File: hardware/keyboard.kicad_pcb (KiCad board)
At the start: 2 copper layers, 166 parts, among them J1 USB_OTG, J10 PD5, J11 PD6, J12 PD7, J13 PE6, J14 PF0, J15 PF1, J16 PF4, J17 PF5, J18 PF6, J19 PF7, J2 PB5, J3 PB6, J4 PB7, J5 PC6, J6 PC7, J7 PD2, J8 PD3, J9 PD4, U1 ATMEGA32U4-AU, U2 MCP23018_SSOP, Y1 16MHz

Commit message: Fix diodes, Add board edge
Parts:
- moved J1 77.1 mm to (179.0, 34.1), turned to 180 degrees
- moved F1 69.3 mm to (187.6, 47.8)
- moved C2 67.2 mm to (190.6, 52.6)
- moved S100 59.0 mm to (161.5, 47.4)
- moved U1 54.7 mm to (179.0, 59.6), turned to 180 degrees
- moved J2 51.9 mm to (197.8, 88.8)
- moved C1 32.5 mm to (177.6, 119.4)
- moved U2 31.1 mm to (178.6, 112.8), turned to 90 degrees
- moved R1 27.7 mm to (175.6, 99.4)
- moved D61 13.0 mm to (145.6, 141.5), turned to 350 degrees
- moved D64 12.9 mm to (199.6, 143.7), turned to 10 degrees
- moved D56 2.09 mm to (310.2, 37.9)
- moved D33 2.09 mm to (222.7, 90.0)
- moved D34 2.09 mm to (226.0, 108.8)
- moved D35 2.09 mm to (229.3, 127.5)
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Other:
- board outline added: 321.6 x 127.7 mm

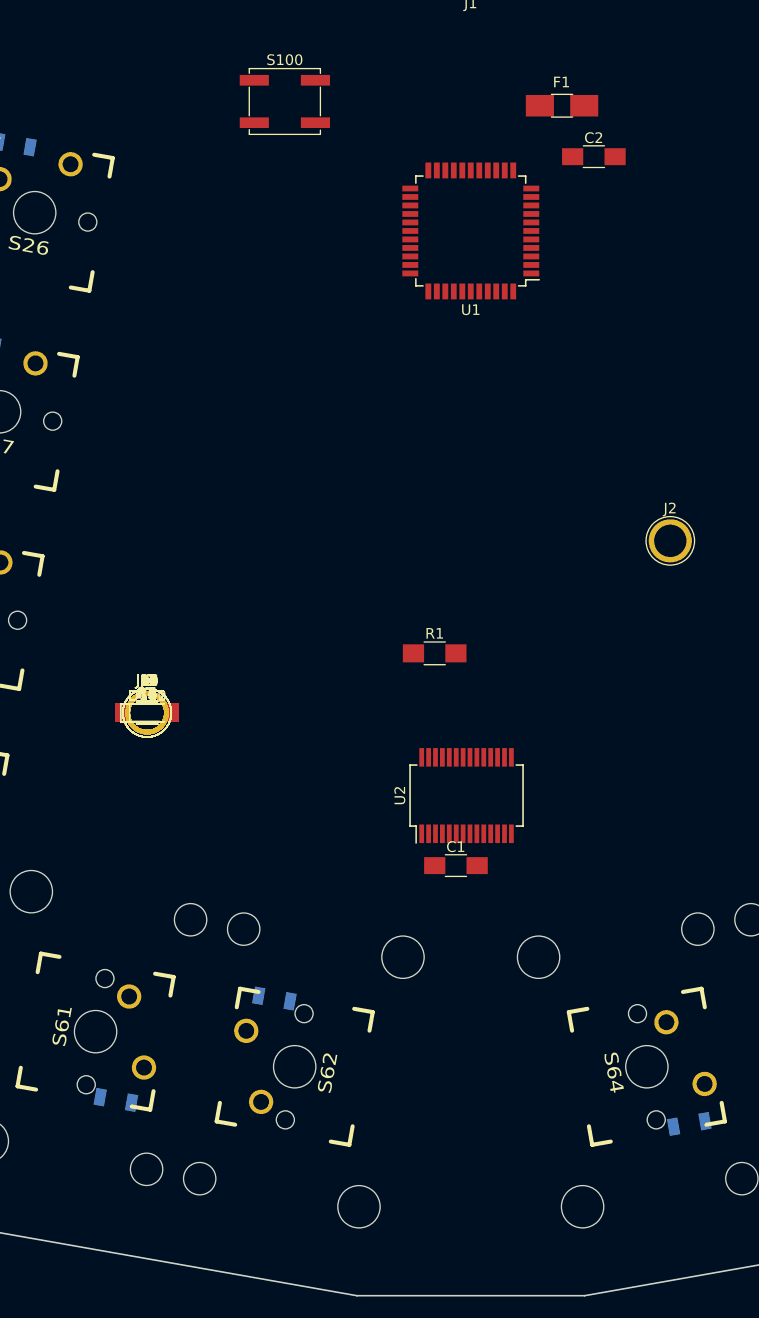
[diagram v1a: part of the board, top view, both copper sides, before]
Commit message: Update expansion pads to be SMD
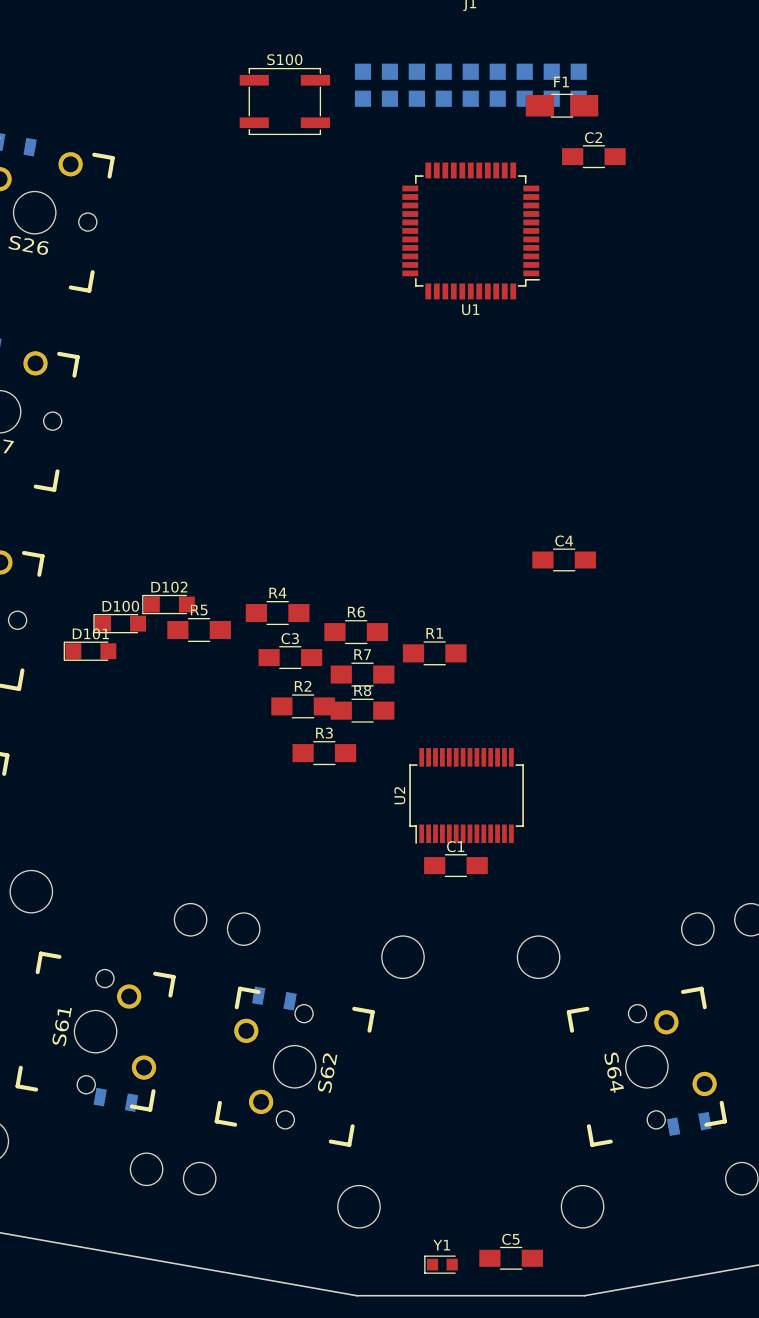
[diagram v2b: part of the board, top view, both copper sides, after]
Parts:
- removed J10: PD5, Connectors:1pin
- removed J11: PD6, Connectors:1pin
- removed J12: PD7, Connectors:1pin
- removed J13: PE6, Connectors:1pin
- removed J14: PF0, Connectors:1pin
- removed J15: PF1, Connectors:1pin
- removed J16: PF4, Connectors:1pin
- removed J17: PF5, Connectors:1pin
- removed J18: PF6, Connectors:1pin
- removed J19: PF7, Connectors:1pin
- removed J3: PB6, Connectors:1pin
- removed J4: PB7, Connectors:1pin
- removed J5: PC6, Connectors:1pin
- removed J6: PC7, Connectors:1pin
- removed J7: PD2, Connectors:1pin
- removed J8: PD3, Connectors:1pin
- removed J9: PD4, Connectors:1pin
- added C4: 100nF, Capacitors_SMD:C_1206_HandSoldering, F.Cu at (187.8, 90.6)
- added C5: 100nF, Capacitors_SMD:C_1206_HandSoldering, F.Cu at (182.8, 156.4)
- J2: value PB5 -> CONN_02X09; footprint Connectors:1pin -> keyboard-modules:pads; moved to B.Cu
- moved Y1 59.0 mm to (176.3, 157.0)
- moved J2 46.9 mm to (179.0, 45.9)
- moved R6 21.1 mm to (168.2, 97.4)
- moved R7 20.6 mm to (168.8, 101.4)
- moved R8 20.3 mm to (168.8, 104.8)
- moved R3 17.1 mm to (165.2, 108.8)
- moved R4 15.5 mm to (160.8, 95.6)
- moved R2 14.7 mm to (163.2, 104.4)
- moved C3 14.5 mm to (162.0, 99.8)
- moved D102 10.4 mm to (150.6, 94.8)
- moved R5 9.21 mm to (153.4, 97.2)
- moved D100 8.77 mm to (146.0, 96.6)
- moved D101 7.86 mm to (143.2, 99.2)
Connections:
- J2 pad 1: /PB5 -> /PF7

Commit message: Add 3d models
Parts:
- J2: moved to F.Cu
- moved C5 159.1 mm to (146.3, 1.59)
- moved Y1 144.4 mm to (206.5, 15.8)
- moved U2 114.8 mm to (136.3, 6.09), turned to 0 degrees
- moved R7 113.2 mm to (203.2, -6.42)
- moved R2 112.7 mm to (204.1, -0.62)
- moved D101 107.4 mm to (203.5, 10.3)
- moved C1 106.2 mm to (194.7, 14.6)
- moved D102 104.3 mm to (203.5, 4.92)
- moved R5 103.8 mm to (197.2, 3.08)
- moved C3 100.8 mm to (190.2, 2.98)
- moved R8 99.7 mm to (183.3, 6.12)
- moved D100 97.9 mm to (201.0, 15.6)
- moved R4 97.9 mm to (183.3, 0.33)
- moved R3 96.8 mm to (187.7, 14.7)
- moved R1 93.1 mm to (197.2, 8.88)
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
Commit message: Start to lay out components
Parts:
- removed D100, D102: LED, LEDs:LED_1206
- D101: value LED -> LED_RGB; footprint LEDs:LED_1206 -> LEDs:LED_RGB_5050-6
- J2: value CONN_02X09 -> CONN_02X10; footprint keyboard-modules:pads -> keyboard-modules:ExpansionPads; moved to B.Cu
- R8: moved to B.Cu
- moved R5 113.0 mm to (171.0, 113.0)
- moved U2 111.6 mm to (179.1, 109.2)
- moved R4 111.0 mm to (171.0, 110.6)
- moved C5 106.4 mm to (171.2, 105.0), turned to 180 degrees
- moved C3 80.2 mm to (169.4, 80.4), turned to 180 degrees
- moved C1 78.9 mm to (180.1, 92.1), turned to 270 degrees
- moved C2 78.8 mm to (177.9, 92.1), turned to 270 degrees
- moved Y1 77.1 mm to (179.0, 87.9), turned to 180 degrees
- moved R8 74.3 mm to (181.9, 80.4), turned to 90 degrees
- moved U1 73.3 mm to (179.5, 80.4)
- moved J2 64.8 mm to (217.2, 37.3), turned to 180 degrees
- moved C4 64.0 mm to (169.4, 77.2), turned to 180 degrees
- moved R7 53.4 mm to (178.8, 41.1), turned to 90 degrees
- moved F1 47.3 mm to (181.9, 41.1), turned to 90 degrees
- moved J1 41.7 mm to (179.1, 34.2), turned to 180 degrees
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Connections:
- net +3V3 renamed Net-(C3-Pad1)
- D101 pad 1: GND -> Net-(D101-Pad1)
- J2 pad 1: /PF7 -> VCC
- J2 pad 10: /PC7 -> /PD2
- J2 pad 11: /PF0 -> /PF1
- J2 pad 12: /PD2 -> /PD3
- J2 pad 13: /PE6 -> /PF0
- J2 pad 14: /PD3 -> /PD4
- J2 pad 15: /PD7 -> /PE6
- J2 pad 16: /PD4 -> /PD5
- J2 pad 17: /PD6 -> /PD7
- J2 pad 18: /PD5 -> /PD6
- J2 pad 2: /PB5 -> GND
- J2 pad 3: /PF6 -> /PF7
- J2 pad 4: /PB6 -> GND
- J2 pad 5: /PF5 -> /PF6
- J2 pad 6: /PB7 -> /PC6
- J2 pad 7: /PF4 -> /PF5
- J2 pad 8: /PC6 -> /PC7
- J2 pad 9: /PF1 -> /PF4
- R1 pad 1: +5V -> Net-(D101-Pad1)
- R1 pad 2: Net-(D100-Pad2) -> GND
- R2 pad 1: (no net) -> Net-(D101-Pad2)
- R2 pad 2: Net-(D101-Pad2) -> GND
- R3 pad 1: (no net) -> Net-(D101-Pad3)
- R3 pad 2: Net-(D102-Pad2) -> GND
- U1 pad 12: /PB7 -> LED3
- U1 pad 29: /PB5 -> LED1
- U1 pad 30: /PB6 -> LED2

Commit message: Start routing
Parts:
- moved S100 3.38 mm to (168.7, 38.6)
- moved R8 0.52 mm to (182.4, 80.5)
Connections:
- U2 pad 17: COL8 -> COL6
- U2 pad 18: COL9 -> COL7
- U2 pad 19: COL10 -> COL8
- U2 pad 20: COL11 -> COL9
- U2 pad 21: COL12 -> COL10
- U2 pad 22: (no net) -> COL11
- U2 pad 23: (no net) -> COL12
- U2 pad 8: COL6 -> (no net)
- U2 pad 9: COL7 -> (no net)
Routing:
- net /KEYS/KCEB/ROW: track 0.00 -> 208.9 mm
- net ROW3: track 0.00 -> 153.3 mm
- net ROW0: track 0.00 -> 146.4 mm
- net ROW1: track 0.00 -> 143.7 mm
- net ROW2: track 0.00 -> 142.3 mm
- net COL4: track 0.00 -> 80.5 mm
- net COL3: track 0.00 -> 80.5 mm
- net COL2: track 0.00 -> 80.5 mm
- net COL5: track 0.00 -> 80.5 mm
- net COL1: track 0.00 -> 80.5 mm
- net COL0: track 0.00 -> 80.5 mm
- net COL11: track 0.00 -> 21.8 mm
- net COL9: track 0.00 -> 21.8 mm
- net COL10: track 0.00 -> 21.6 mm
- net Net-(D19-Pad2): track 0.00 -> 7.01 mm
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
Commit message: More routing
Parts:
- removed J2: CONN_02X10, keyboard-modules:ExpansionPads
- moved D63 8.85 mm to (209.2, 138.4), turned to 280 degrees
- moved D64 8.82 mm to (200.8, 135.0), turned to 100 degrees
- moved D62 8.65 mm to (156.5, 139.6), turned to 260 degrees
- moved D61 8.62 mm to (149.6, 133.9), turned to 80 degrees
- moved C5 2.87 mm to (173.2, 103.0)
- moved U2 0.28 mm to (179.1, 108.9)
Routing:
- net ROW3: track 153.3 -> 393.5 mm, vias 0 -> 3
- net ROW2: track 142.3 -> 378.6 mm, vias 0 -> 3
- net ROW0: track 146.4 -> 324.3 mm, vias 0 -> 1
- net ROW1: track 143.7 -> 305.1 mm, vias 0 -> 1
- net COL12: track 0.00 -> 110.4 mm, vias 0 -> 3
- net COL8: track 0.00 -> 107.7 mm
- net COL6: track 0.00 -> 107.7 mm
- net COL7: track 0.00 -> 107.3 mm
- net /KEYS/KCEB/ROW: track 208.9 -> 309.1 mm
- net COL10: track 21.6 -> 108.1 mm
- net COL11: track 21.8 -> 107.8 mm
- net COL9: track 21.8 -> 107.3 mm
- net LED3: track 0.00 -> 65.4 mm, vias 0 -> 2
- net Net-(S100-Pad2): track 0.00 -> 51.8 mm, vias 0 -> 2
- net LED2: track 0.00 -> 46.5 mm, vias 0 -> 2
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
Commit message: more routing progress
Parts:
- moved R5 0.38 mm to (171.0, 112.6)
- moved R4 0.25 mm to (171.0, 110.4)
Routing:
- net COL0: track 106.1 -> 263.6 mm, vias 0 -> 3
- net COL11: track 107.8 -> 258.6 mm, vias 0 -> 3
- net COL1: track 106.1 -> 230.5 mm, vias 0 -> 3
- net ROW2: track 378.6 -> 496.3 mm
- net COL10: track 108.1 -> 225.0 mm, vias 0 -> 3
- net COL9: track 107.3 -> 197.4 mm, vias 0 -> 3
- net COL2: track 106.3 -> 195.7 mm, vias 0 -> 3
- net +5V: track 23.6 -> 97.6 mm, vias 3 -> 9
- net ROW0: track 324.3 -> 397.1 mm, vias 1 -> 2
- net COL3: track 106.0 -> 175.5 mm, vias 0 -> 1
- net COL8: track 107.7 -> 170.0 mm, vias 0 -> 3
- net ROW1: track 305.1 -> 366.9 mm, vias 1 -> 2
- net COL4: track 106.1 -> 153.9 mm, vias 0 -> 1
- net COL7: track 107.3 -> 143.8 mm, vias 0 -> 1
- net COL5: track 106.0 -> 135.6 mm, vias 0 -> 1
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
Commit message: More routing
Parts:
- moved C5 5.88 mm to (179.1, 102.4), turned to 0 degrees
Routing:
- net GND: track 0.00 -> 181.3 mm, vias 0 -> 10
- net ROW2: track 496.3 -> 369.1 mm
- net COL11: track 258.6 -> 226.3 mm, vias 3 -> 1
- net +5V: track 97.6 -> 73.7 mm, vias 9 -> 7
- net COL10: track 225.0 -> 207.0 mm, vias 3 -> 1
- net COL9: track 197.4 -> 185.7 mm, vias 3 -> 1
- net VCC: track 19.9 -> 30.5 mm
- net Net-(J1-Pad6): track 13.2 -> 19.4 mm
- net COL8: track 170.0 -> 166.0 mm, vias 3 -> 1
- net LED3: track 65.3 -> 69.1 mm
- net Net-(S100-Pad2): track 57.6 -> 54.5 mm
- net COL2: track 195.7 -> 198.3 mm
- net COL0: track 263.6 -> 265.7 mm
- net ROW0: track 397.1 -> 395.2 mm
- net Net-(R6-Pad1): track 39.1 -> 40.6 mm
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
